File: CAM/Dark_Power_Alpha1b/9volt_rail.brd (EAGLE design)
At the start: 94.9 x 67.3 mm, 48 parts, among them IC1 TL331

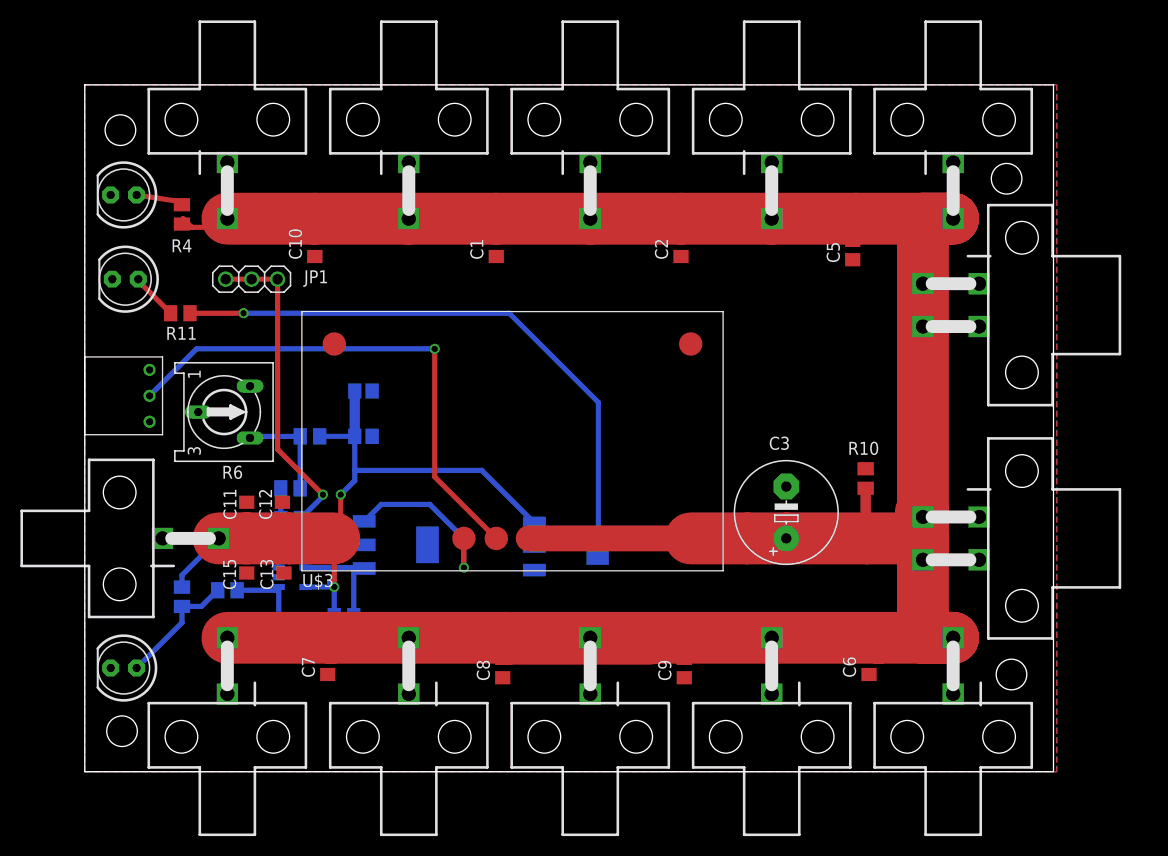
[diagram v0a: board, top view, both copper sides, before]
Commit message: Update to dark power and update to ADC cape
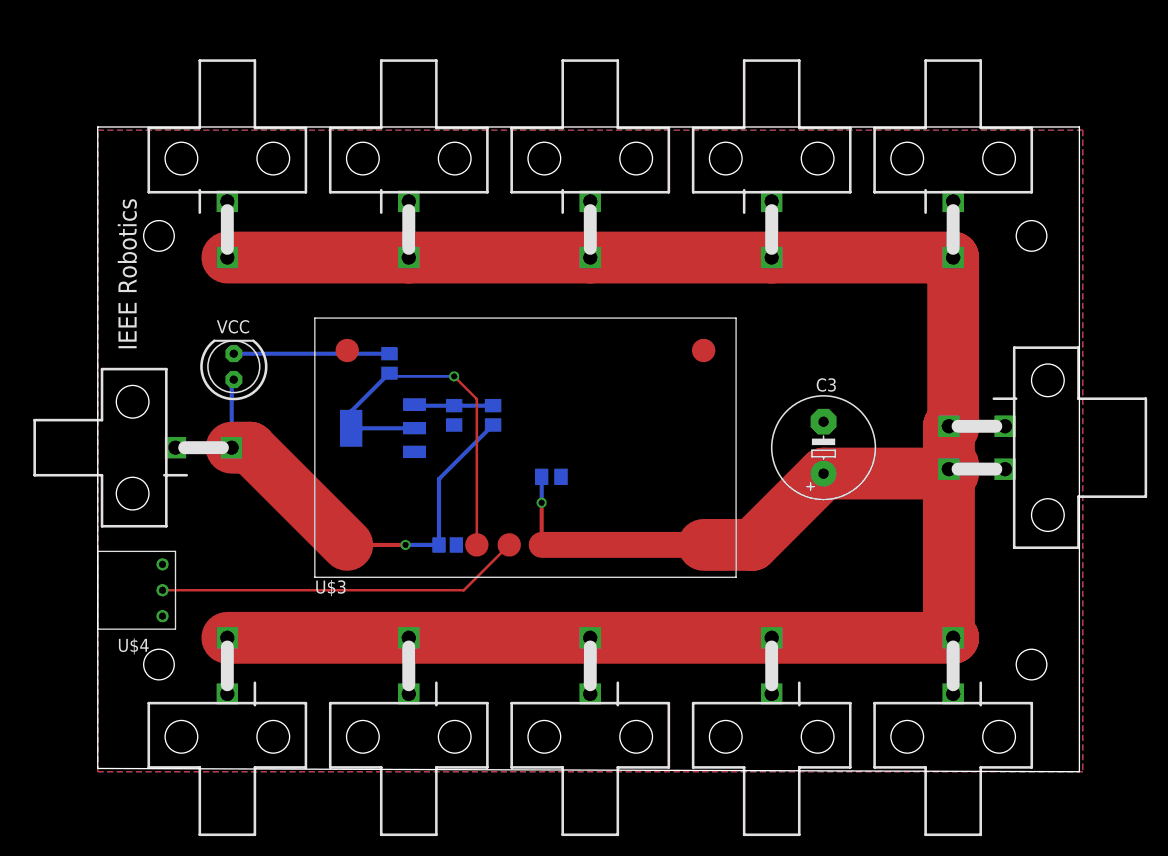
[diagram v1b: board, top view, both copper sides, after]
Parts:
- removed C1, C10, C2, C5, C6, C7, C8, C9: (no value), rcl:C0805
- removed C11, C12, C13, C14, C15: 2.2uF, adafruit:C0805
- removed IC1: TL331, linear:DBV-R-PDSO-G5
- removed JP1: (no value), adafruit:1X03
- removed PL13: (no value), con-molex-2:5569-4
- removed R1, R10, R11, R3, R5, R7: (no value), adafruit:M0805
- removed R6: (no value), pot:RS3
- removed T1: (no value), zetex:SOT223
- removed VCC1, VCC2, VCC3: (no value), adafruit:LED5MM
- added VCC: (no value), adafruit:LED5MM
- moved PL6 85.9 mm to (12.7, 55.9), turned to 180 degrees
- moved PL1 71.9 mm to (66.0, 55.9), turned to 180 degrees
- moved PL2 71.9 mm to (83.8, 55.9), turned to 180 degrees
- moved PL5 63.1 mm to (83.8, 7.62), turned to 0 degrees
- moved PL4 59.9 mm to (30.5, 55.9), turned to 180 degrees
- moved PL7 55.0 mm to (66.0, 7.62), turned to 0 degrees
- moved PL8 55.0 mm to (48.3, 7.62), turned to 0 degrees
- moved PL10 52.1 mm to (12.7, 7.62), turned to 0 degrees
- moved PL9 52.1 mm to (30.5, 7.62), turned to 0 degrees
- moved PL3 48.3 mm to (48.3, 55.9), turned to 180 degrees
- moved R4 44.4 mm to (44.5, 28.9), flipped to the bottom, turned to 180 degrees
- moved R8 24.5 mm to (38.7, 34.9), turned to 90 degrees
- moved U$4 19.1 mm to (6.35, 17.8)
- moved R9 19.0 mm to (34.9, 34.9), turned to 270 degrees
- moved R2 15.6 mm to (28.6, 40.0), turned to 270 degrees
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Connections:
- removed net N$10: R11.1, T1.2, T1.4
- removed net N$2: IC1.4, JP1.1, JP1.2, JP1.3, R8.1, R9.2, T1.1, T3.1
- removed net N$3: R1.2, R5.1, VCC1.A
- removed net N$6: R2.1, R3.2, R6.E
- removed net N$7: IC1.1, R5.2, R7.1
- removed net N$8: R11.2, VCC3.A
- removed net N$9: R4.2, VCC2.A
- new net N$14: R8.2, R9.1, T3.1
- net GND: now also R4.2, R9.2, T3.3; no longer C1.1, C10.1, C11.2, C12.2, C13.2, C14.2, C15.2, C2.1, C5.1, C6.1, C7.1, C8.1, C9.1, IC1.2, PL13.1, PL13.2, R10.2, R6.S, R7.2, T3.2, T3.4, VCC1.K, VCC2.K, VCC3.K
- net N$1: no longer C1.2, C10.2, C2.2, C5.2, C6.2, C7.2, C8.2, C9.2, PL13.3, PL13.4, R10.1
- net N$4: now also R2.1, VCC.K; no longer IC1.3, R2.2, R9.1
- net N$5: now also R2.2, T3.2, T3.4; no longer T3.3
- net VCC: now also R8.1, VCC.A; no longer C11.1, C12.1, C13.1, C14.1, C15.1, IC1.5, R1.1, R3.1, R8.2, T1.3
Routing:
- net N$10: track 64.0 -> 0.00 mm, vias 1 -> 0
- net N$2: track 47.1 -> 0.00 mm, vias 1 -> 0
- net N$1: track 273.0 -> 231.4 mm, vias 0 -> 1
- net VCC: track 75.2 -> 45.1 mm, vias 2 -> 1
- net N$5: track 17.5 -> 37.1 mm
- net N$12: track 50.9 -> 35.8 mm, vias 1 -> 0
- net N$3: track 12.0 -> 0.00 mm
- net N$6: track 10.1 -> 0.00 mm
- net N$7: track 8.50 -> 0.00 mm
- net N$14: track 0.00 -> 7.73 mm
- net N$4: track 7.84 -> 15.2 mm
- net N$8: track 4.65 -> 0.00 mm
- net N$9: track 4.63 -> 0.00 mm
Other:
- board size 94.9 x 67.3 mm -> 96.2 x 63.2 mm
- board text added: "IEEE Robotics"
